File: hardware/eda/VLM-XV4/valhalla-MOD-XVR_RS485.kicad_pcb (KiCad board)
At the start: 2 copper layers, 76.2 x 50.8 mm, 5 parts, among them J1 BUS

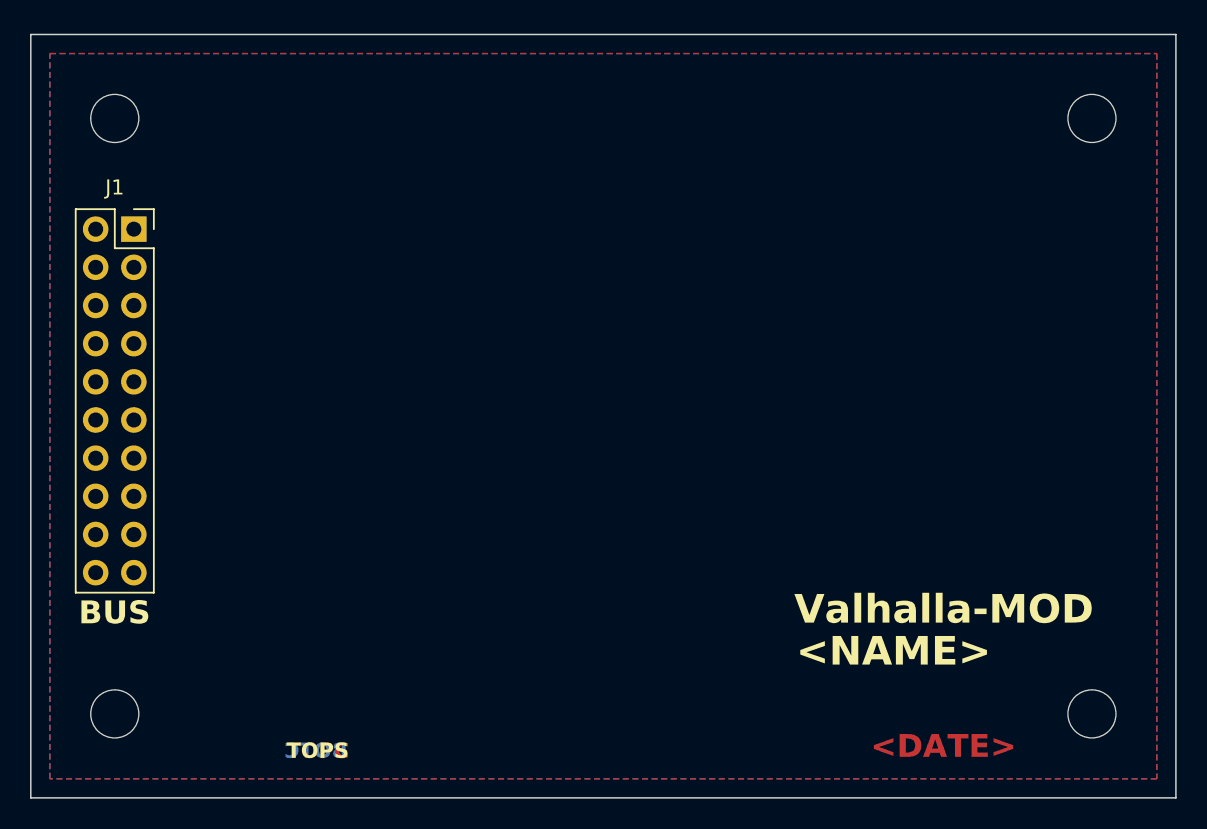
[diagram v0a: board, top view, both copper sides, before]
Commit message: UPDATE: finalized schematic of XVR(RS485)
  - found a solution for Vio transparency using a buck-boost regulator
    module, this in turn opened the way to cheap 5V-powered RS485
    transceivers.
  - done initial component placement on the PCB, routing to follow.
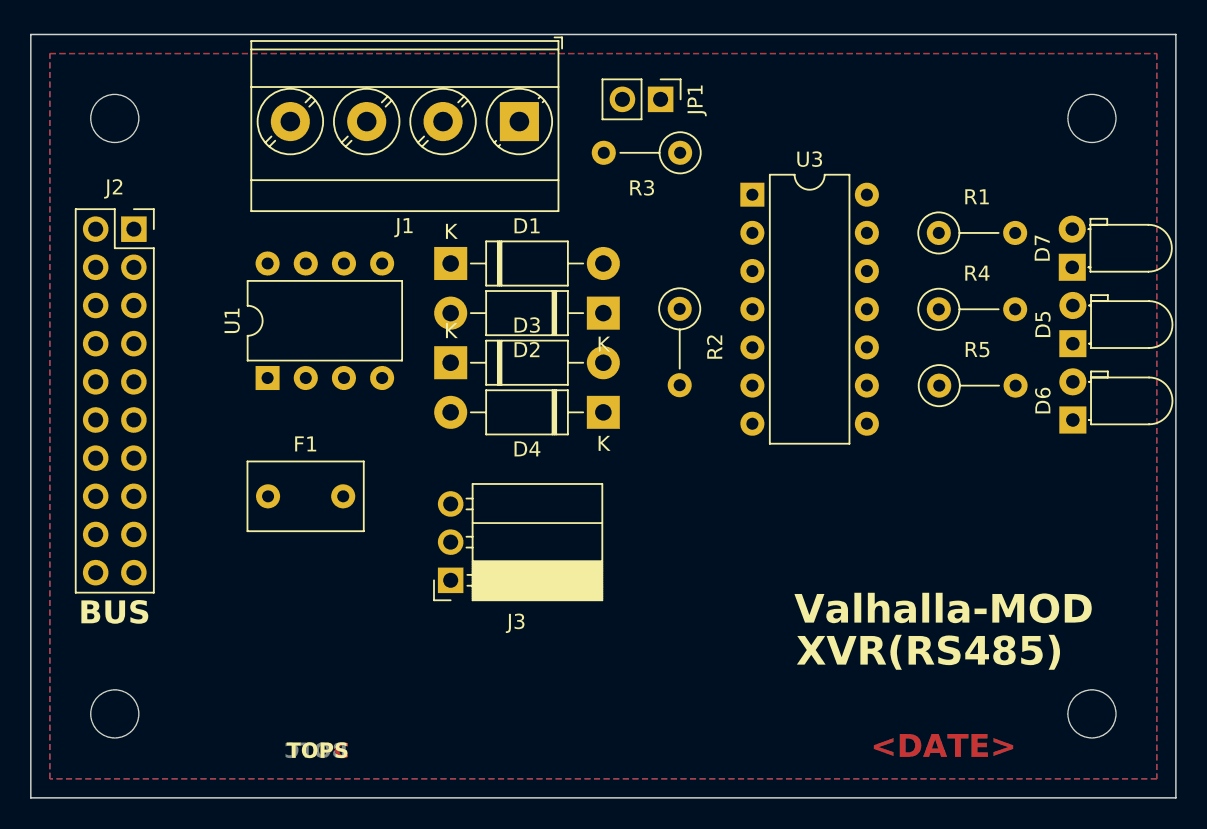
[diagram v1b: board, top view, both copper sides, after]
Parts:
- added D1: 12V, Diode_THT:D_DO-41_SOD81_P10.16mm_Horizontal, F.Cu at (96.5, 50.8)
- added D2: 7V, Diode_THT:D_DO-41_SOD81_P10.16mm_Horizontal, F.Cu at (106.7, 54.1)
- added D3: 12V, Diode_THT:D_DO-41_SOD81_P10.16mm_Horizontal, F.Cu at (96.5, 57.4)
- added D4: 7V, Diode_THT:D_DO-41_SOD81_P10.16mm_Horizontal, F.Cu at (106.7, 60.7)
- added D5: *2, LED_THT:LED_D3.0mm_Horizontal_O1.27mm_Z2.0mm, F.Cu at (137.9, 56.1)
- added D6: *2, LED_THT:LED_D3.0mm_Horizontal_O1.27mm_Z2.0mm, F.Cu at (137.9, 61.2)
- added D7: LED, LED_THT:LED_D3.0mm_Horizontal_O1.27mm_Z2.0mm, F.Cu at (137.9, 51.1)
- added F1: 250mA, Capacitor_THT:C_Disc_D7.5mm_W4.4mm_P5.00mm, F.Cu at (84.4, 66.3)
- added J1: ModBUS, TerminalBlock_Phoenix:TerminalBlock_Phoenix_MKDS-3-4-5.08_1x04_P5.08mm_Horizontal, F.Cu at (101.1, 41.4)
- added J3: POLOLU-4941, Connector_PinSocket_2.54mm:PinSocket_1x03_P2.54mm_Horizontal, F.Cu at (96.5, 71.9)
- added JP1: TERMINATION, Connector_PinHeader_2.54mm:PinHeader_1x02_P2.54mm_Vertical, F.Cu at (110.5, 39.9)
- added R1: *3, Resistor_THT:R_Axial_DIN0207_L6.3mm_D2.5mm_P5.08mm_Vertical, F.Cu at (129.0, 48.8)
- added R2: 10K, Resistor_THT:R_Axial_DIN0207_L6.3mm_D2.5mm_P5.08mm_Vertical, F.Cu at (111.8, 53.8)
- added R3: 120R, Resistor_THT:R_Axial_DIN0207_L6.3mm_D2.5mm_P5.08mm_Vertical, F.Cu at (111.8, 43.4)
- added R4: *1, Resistor_THT:R_Axial_DIN0207_L6.3mm_D2.5mm_P5.08mm_Vertical, F.Cu at (129.0, 53.8)
- added R5: *1, Resistor_THT:R_Axial_DIN0207_L6.3mm_D2.5mm_P5.08mm_Vertical, F.Cu at (129.0, 58.9)
- added U1: *1, Package_DIP:DIP-8_W7.62mm, F.Cu at (84.3, 58.4)
- added U3: 74LS06, Package_DIP:DIP-14_W7.62mm, F.Cu at (116.6, 46.2)
- renumbered J1 to J2
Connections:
- J2 pad 1: /AVCC -> unconnected-(J2-Pin_1-Pad1)
- J2 pad 10: /~{SS} -> unconnected-(J2-Pin_10-Pad10)
- J2 pad 11: /~{SINT} -> unconnected-(J2-Pin_11-Pad11)
- J2 pad 13: /SDA -> unconnected-(J2-Pin_13-Pad13)
- J2 pad 14: /SCL -> unconnected-(J2-Pin_14-Pad14)
- J2 pad 15: /~{IINT} -> unconnected-(J2-Pin_15-Pad15)
- J2 pad 2: /AGND -> unconnected-(J2-Pin_2-Pad2)
- J2 pad 20: /~{DCD} -> unconnected-(J2-Pin_20-Pad20)
- J2 pad 5: /~{RESET} -> unconnected-(J2-Pin_5-Pad5)
- J2 pad 7: /MOSI -> unconnected-(J2-Pin_7-Pad7)
- J2 pad 8: /MISO -> unconnected-(J2-Pin_8-Pad8)
- J2 pad 9: /SCK -> unconnected-(J2-Pin_9-Pad9)
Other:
- board text added: "XVR(RS485)"
- board text removed: "<NAME>"

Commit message: UPDATE: XVR(RS485) RTM and XVR(RS232) started
  - after the final cosmetic tweaks, XVR(RS485) has reached RTM status
  - started work on XVR(RS232), schematic is mostly done -- save for
    the UI.
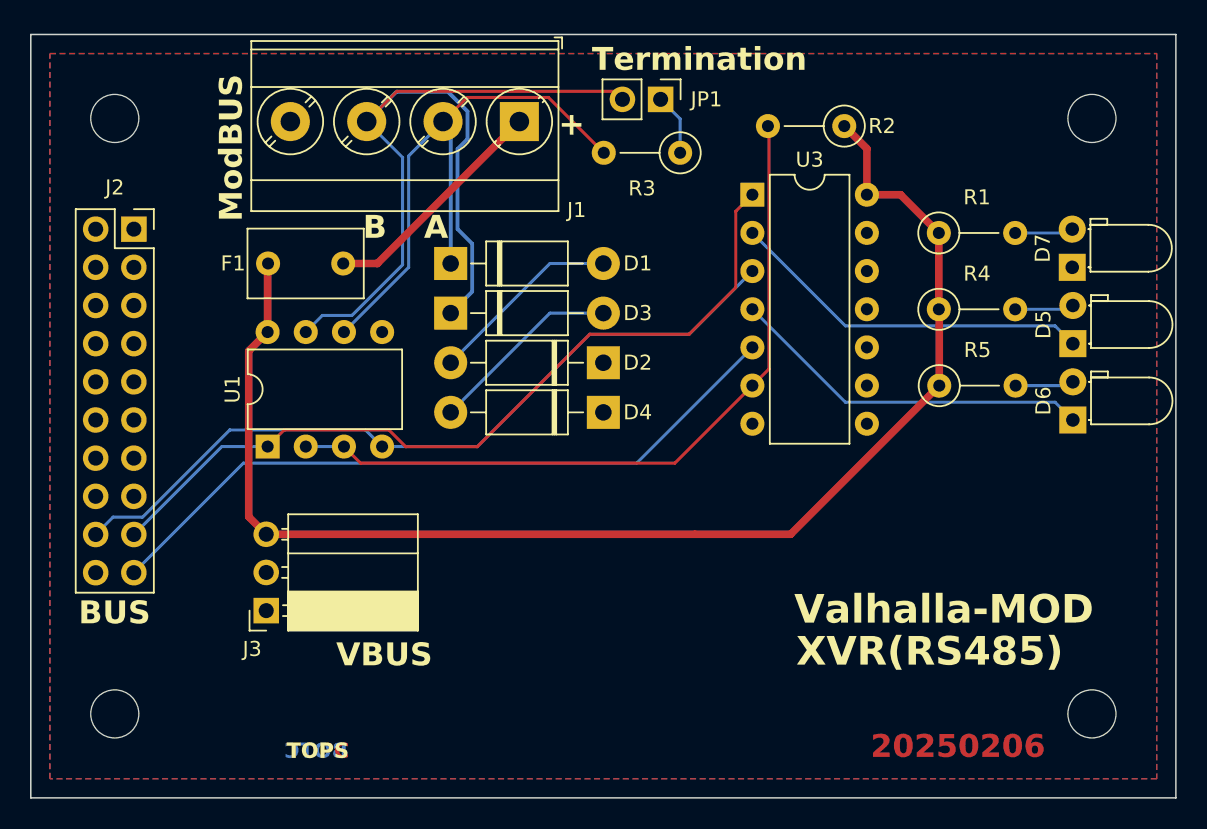
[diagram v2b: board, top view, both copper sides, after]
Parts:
- moved R2 16.4 mm to (122.7, 41.7), turned to 180 degrees
- moved F1 15.5 mm to (84.4, 50.8)
- moved J3 12.4 mm to (84.2, 73.9)
- moved U1 4.56 mm to (84.3, 63.0)
- moved D2 3.30 mm to (106.7, 57.4)
- moved D3 3.30 mm to (96.5, 54.1)
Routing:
- net /LVCC: track 0.00 -> 89.0 mm
- net /RS485_P: track 0.00 -> 59.7 mm
- net /RXDI: track 0.00 -> 54.4 mm
- net /TXDO: track 0.00 -> 51.9 mm
- net Net-(U1-DE): track 0.00 -> 50.1 mm
- net /~{RTS}: track 0.00 -> 47.4 mm
- net /RS485_N: track 0.00 -> 38.6 mm
- net Net-(D5-K): track 0.00 -> 24.4 mm
- net Net-(D6-K): track 0.00 -> 24.4 mm
- net Net-(J1-Pin_1): track 0.00 -> 15.6 mm
- net Net-(D3-A): track 0.00 -> 12.9 mm
- net Net-(D1-A): track 0.00 -> 12.9 mm
- net Net-(JP1-A): track 0.00 -> 4.09 mm
- net Net-(D5-A): track 0.00 -> 3.59 mm
- net Net-(D6-A): track 0.00 -> 3.56 mm
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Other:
- board text added: "+"
- board text added: "20250206"
- board text added: "A"
- board text added: "B"
- board text added: "ModBUS"
- board text added: "Termination"
- board text added: "VBUS"
- board text removed: "<DATE>"

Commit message: UPDATE: updated MOD-XVR(RS485) to the latest specification.
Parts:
- removed D7: LED, LED_THT:LED_D3.0mm_Horizontal_O1.27mm_Z2.0mm
- removed J3: POLOLU-4941, Connector_PinSocket_2.54mm:PinSocket_1x03_P2.54mm_Horizontal
- removed R1: *3, Resistor_THT:R_Axial_DIN0207_L6.3mm_D2.5mm_P5.08mm_Vertical
- D5, D6: value *2 -> R
- R4, R5: value *1 -> *3
- moved D5 5.08 mm to (137.9, 51.1)
- moved D6 5.08 mm to (137.9, 56.1)
- moved R4 5.08 mm to (129.0, 48.8)
- moved R5 5.08 mm to (129.0, 53.8)
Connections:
- F1 pad 1: /LVCC -> /DVCC
- J2 pad 16: unconnected-(J2-Pin_16-Pad16) -> /LVCC
- J2 pad 6: unconnected-(J2-Pin_6-Pad6) -> /DGND
- R2 pad 1: /LVCC -> /DVCC
- U1 pad 8: /LVCC -> /DVCC
- U3 pad 14: /LVCC -> /DVCC
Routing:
- net /LVCC: track 89.0 -> 81.1 mm
- net Net-(D7-A): track 3.54 -> 0.00 mm
- net Net-(D5-K): track 24.4 -> 22.3 mm
- net Net-(D6-K): track 24.4 -> 22.3 mm
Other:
- board text added: "20250325"
- board text removed: "20250206"
- board text removed: "VBUS"
